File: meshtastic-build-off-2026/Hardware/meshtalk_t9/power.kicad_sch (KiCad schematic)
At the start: 11 parts, among them J1 USB_C_Receptacle_USB2.0_16P, J2 Conn_01x02_Socket, Q1 Q_PMOS_GSD, U2 AP2112K-3.3, U3 MCP73831-2-MC

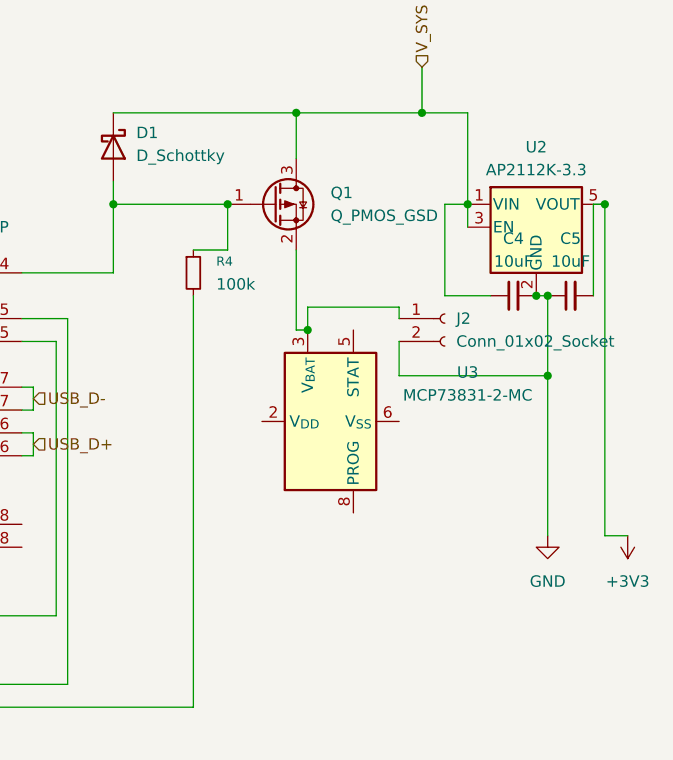
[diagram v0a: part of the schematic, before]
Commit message: rename + battery % + boot btn changed to reset + fix battery chrging
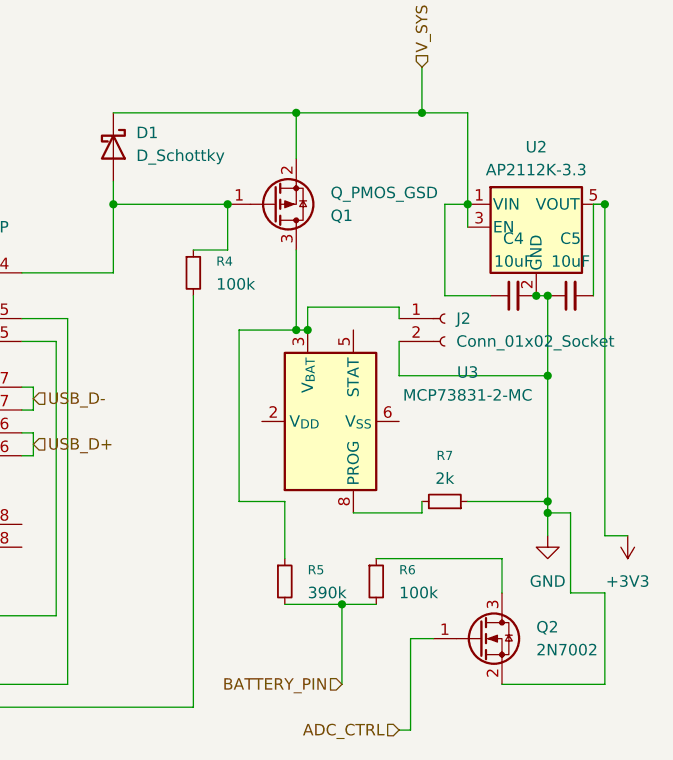
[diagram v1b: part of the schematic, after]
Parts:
- added Q2: 2N7002, Package_TO_SOT_SMD:SOT-23, symbol Transistor_FET:2N7002
- added R5: 390k, Capacitor_SMD:C_0805_2012Metric, symbol Device:R_Small
- added R6: 100k, Capacitor_SMD:C_0805_2012Metric, symbol Device:R_Small
- added R7: 2k, Capacitor_SMD:C_0805_2012Metric, symbol Device:R_Small
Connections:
- net GND: now also Q2.2 (S), R7.1
- net V_SYS: now also Q1.2 (S); no longer Q1.3 (D)
- net at J2.1 (Pin_1), U3.3 (V_{BAT}), U3.4 (V_{BAT}): now also Q1.3 (D), R5.1; no longer Q1.2 (S)
- net at U3.8 (PROG): now also R7.2
- new net: Q2.3 (D), R6.1
- new net ADC_CTRL: Q2.1 (G)
- new net BATTERY_PIN: R5.2, R6.2

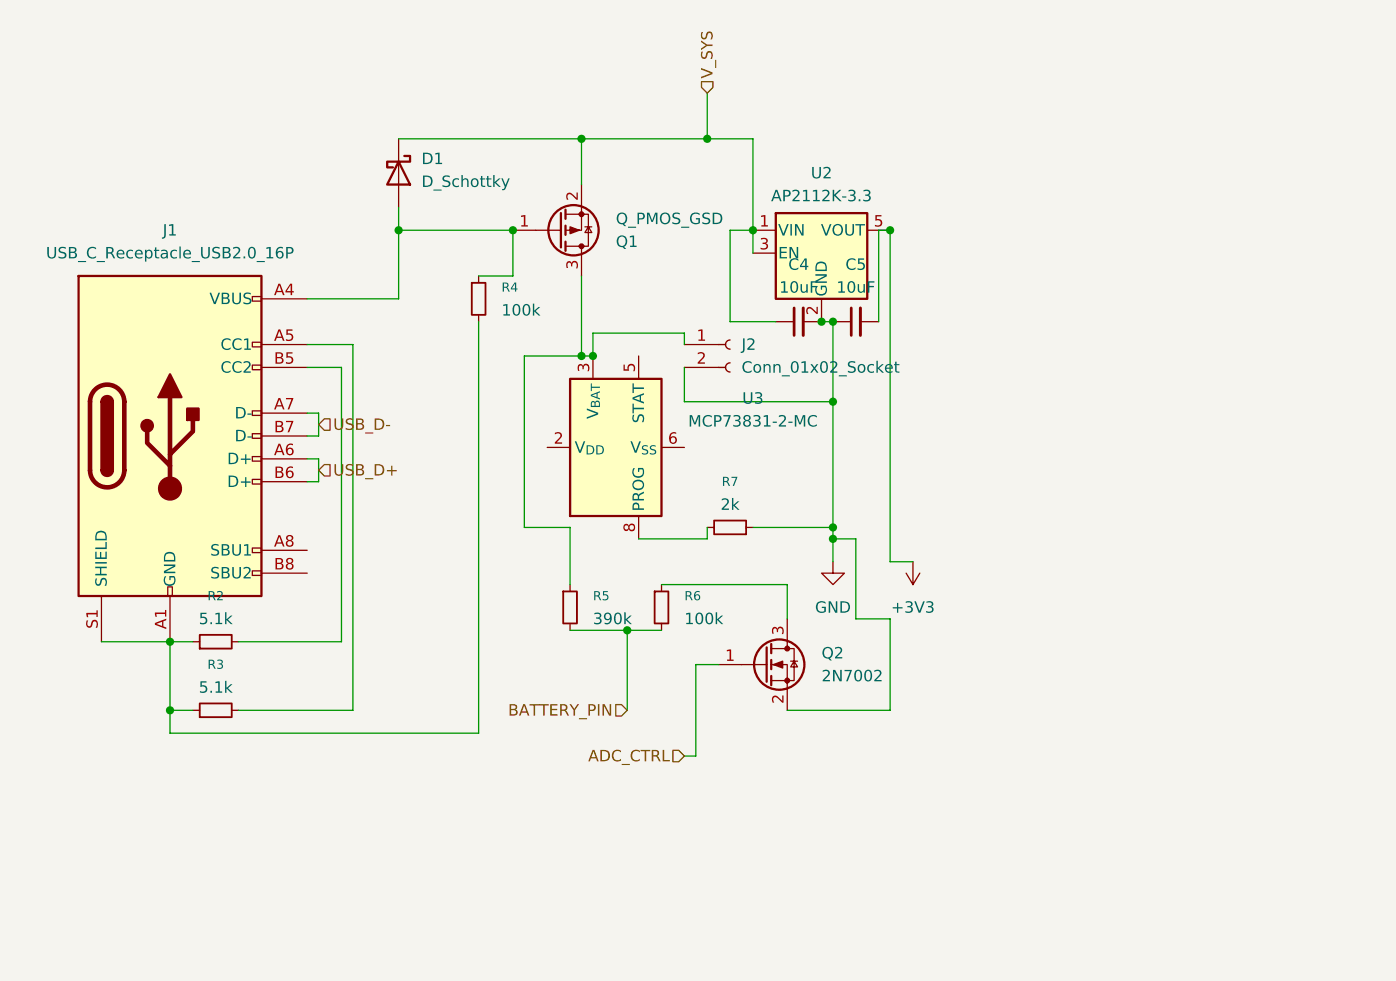
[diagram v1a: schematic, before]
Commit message: Replace AP2112K-3.3  with AP7361C-33E Connected LORA RF_SW1 to GPIO Added ESD Added mounting holes for display (Waveshare 2 inch) Added Boot and Reset buttons made power rails thicker added dedicated layer for 3v3 and GND
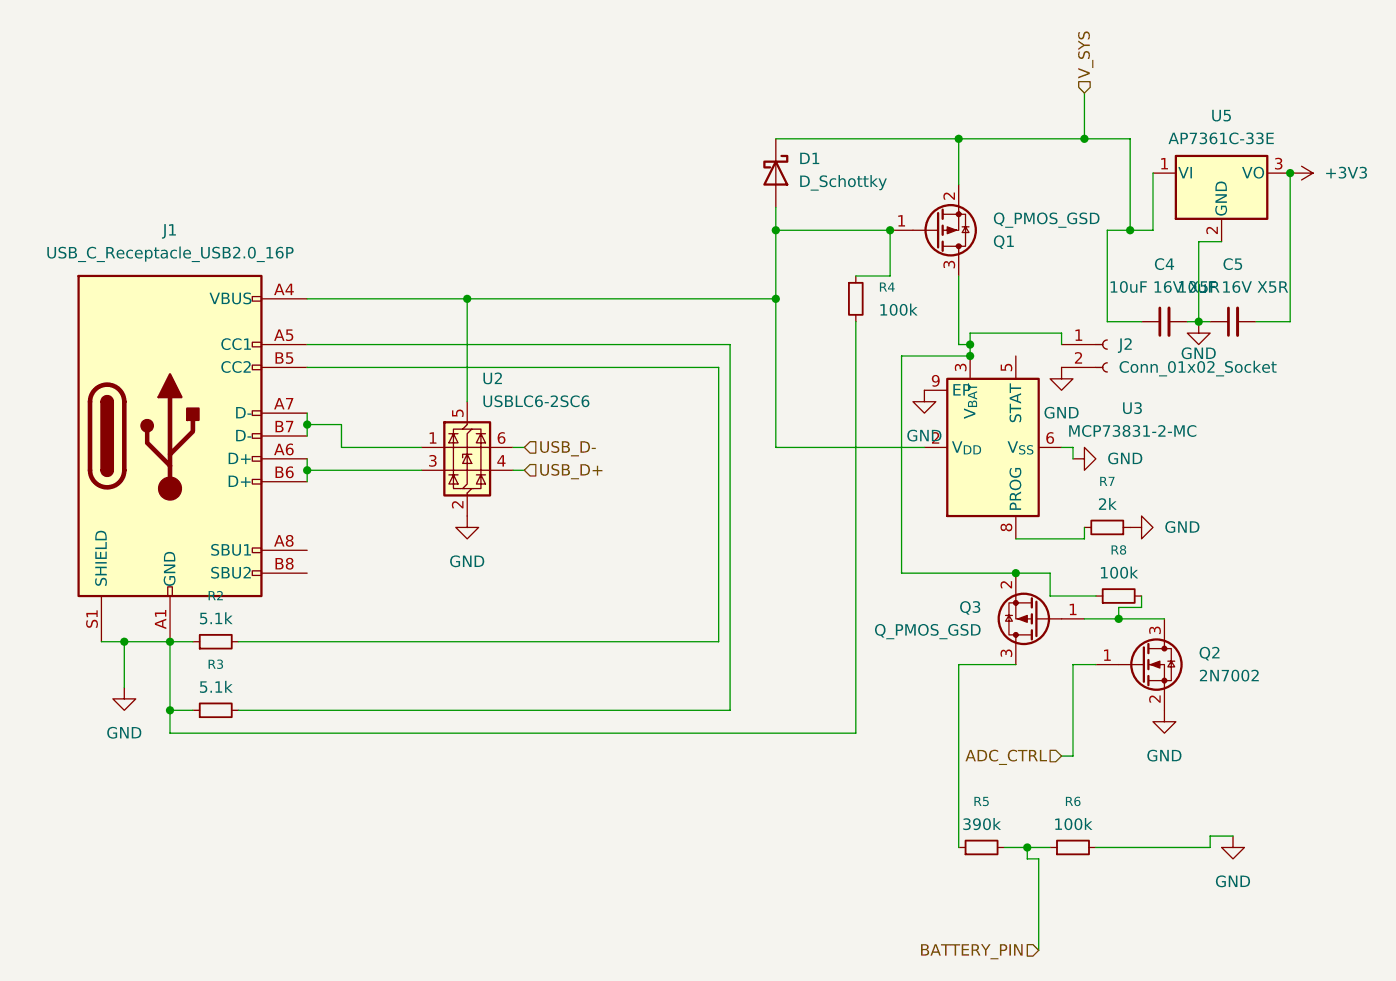
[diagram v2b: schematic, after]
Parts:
- removed U2: AP2112K-3.3, Package_TO_SOT_SMD:SOT-23-5, symbol Regulator_Linear:AP2112K-3.3
- added Q3: Q_PMOS_GSD, Package_TO_SOT_SMD:SOT-23, symbol Transistor_FET:Q_PMOS_GSD
- added R8: 100k, Resistor_SMD:R_0805_2012Metric, symbol Device:R_Small
- added U2: USBLC6-2SC6, Package_TO_SOT_SMD:SOT-23-6, symbol Power_Protection:USBLC6-2SC6
- added U5: AP7361C-33E, Package_TO_SOT_SMD:SOT-223-3_TabPin2, symbol Regulator_Linear:AP7361C-33E
- C4, C5: value 10uF -> 10uF 16V X5R; MPN (none) -> CL21A106KOQNNNE; Manufacturer (none) -> Samsung
- D1: footprint LED_SMD:LED_0805_2012Metric -> Diode_SMD:D_SOD-123; MPN (none) -> MBR0520LT1G; Manufacturer (none) -> onsemi
- J1: MPN (none) -> TYPE-C-31-M-12; Manufacturer (none) -> HROparts
- J2: MPN (none) -> 53261-0271; Manufacturer (none) -> Molex
- Q1: MPN (none) -> AO3401A; Manufacturer (none) -> Alpha & Omega
- Q2: MPN (none) -> 2N7002,215; Manufacturer (none) -> Nexperia
- R2, R3: MPN (none) -> RC0805FR-075K1L; Manufacturer (none) -> YAGEO
- R4: MPN (none) -> RC0805FR-07100KL; Manufacturer (none) -> YAGEO
- R5: footprint Capacitor_SMD:C_0805_2012Metric -> Resistor_SMD:R_0805_2012Metric; MPN (none) -> RC0805FR-07390KL; Manufacturer (none) -> YAGEO
- R6: footprint Capacitor_SMD:C_0805_2012Metric -> Resistor_SMD:R_0805_2012Metric; MPN (none) -> RC0805FR-07100KL; Manufacturer (none) -> YAGEO
- R7: footprint Capacitor_SMD:C_0805_2012Metric -> Resistor_SMD:R_0805_2012Metric; MPN (none) -> RC0805FR-072KL; Manufacturer (none) -> YAGEO
- U3: MPN (none) -> MCP73831T-2ACI/MC; Manufacturer (none) -> Microchip
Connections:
- net +3V3: now also U5.3 (VO)
- net BATTERY_PIN: now also R6.1; no longer R6.2
- net GND: now also J1.A1 (GND), J1.A12 (GND), J1.B1 (GND), J1.B12 (GND), J1.S1 (SHIELD), R2.1, R3.1, R4.2, R6.2, U3.6 (V_{SS}), U3.9 (EP), U2.2 (GND), U5.2 (GND)
- net USB_D+: now also U2.4 (I/O2); no longer J1.A6 (D+), J1.B6 (D+)
- net USB_D-: now also U2.6 (I/O1); no longer J1.A7 (D-), J1.B7 (D-)
- net V_SYS: now also U5.1 (VI)
- net at D1.2 (A), J1.A4 (VBUS), J1.A9 (VBUS)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: now also U3.1 (V_{DD}), U3.2 (V_{DD}), U2.5 (VBUS)
- net at J2.1 (Pin_1), Q1.3 (D), U3.3 (V_{BAT})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: now also Q3.2 (S), R8.1; no longer R5.1
- net at Q2.3 (D): now also Q3.1 (G), R8.2; no longer R6.1
- new net: Q3.3 (D), R5.1
- new net: J1.A7 (D-), J1.B7 (D-), U2.1 (I/O1)
- new net: J1.A6 (D+), J1.B6 (D+), U2.3 (I/O2)
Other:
- moved on the sheet: C4, C5, D1, J2, Q1, Q2, R4, R5, R6, R7
